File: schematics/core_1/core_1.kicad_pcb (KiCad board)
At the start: 2 copper layers, 100 x 91.1 mm, 22 parts, among them U1 74LS00, U2 74LS04, U3 74LS109, U4 74LS02

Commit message: power change
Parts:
- moved C5 1.90 mm to (105.0, 118.2)
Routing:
- net VCC: track 89.9 -> 119.0 mm, vias 1 -> 7
- net GND: track 151.6 -> 153.6 mm
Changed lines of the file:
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@@
 	(footprint "Capacitor_THT:C_Radial_D6.3mm_H5.0mm_P2.50mm"
 		(layer "F.Cu")
-		(at 106.8 118.85 90)
+		(at 105 118.240522 90)
 		(descr "C, Radial series, Radial, pin pitch=2.50mm, diameter=6.3mm, height=5mm, Non-Polar Electrolytic Capacitor")
 		(tags "C Radial series Radial pin pitch 2.50mm diameter 6.3mm height 5mm Non-Polar Electrolytic Capacitor")
@@
 	)
 	(segment
+		(start 104 122.75)
+		(end 104 126.5)
+		(width 0.6)
+		(layer "F.Cu")
+		(net 2)
+	)
+	(segment
+		(start 106 122.75)
+		(end 106 126.5)
+		(width 0.6)
+		(layer "F.Cu")
+		(net 2)
+	)
+	(segment
+		(start 105 122.75)
+		(end 105 126.5)
+		(width 0.6)
+		(layer "F.Cu")
+		(net 2)
+	)
+	(segment
 		(start 190.56 57.05)
 		(end 190.56 53.01)
@@
 	)
 	(segment
+		(start 103.25 122.75)
+		(end 103 123)
+		(width 0.3)
+		(layer "F.Cu")
+		(net 2)
+	)
+	(segment
+		(start 107 122.75)
+		(end 107 126.5)
+		(width 0.6)
+		(layer "F.Cu")
+		(net 2)
+	)
+	(segment
+		(start 105 122.75)
+		(end 105 118.240522)
+		(width 0.6)
+		(layer "F.Cu")
+		(net 2)
+	)
+	(segment
 		(start 178.2 103.2)
 		(end 178.78 102.62)
@@
 	)
 	(segment
+		(start 103 123)
+		(end 103 126.5)
+		(width 0.3)
+		(layer "F.Cu")
+		(net 2)
+	)
+	(segment
 		(start 122 75.68)
 		(end 122 71.65)
@@
 	)
 	(segment
+		(start 107 122.75)
+		(end 103.25 122.75)
+		(width 0.6)
+		(layer "F.Cu")
+		(net 2)
+	)
+	(segment
 		(start 191.7 79.95)
 		(end 191 79.25)
@@
 	)
 	(via
-		(at 105 121.1)
-		(size 0.8)
-		(drill 0.4)
+		(at 104 122.75)
+		(size 0.6)
+		(drill 0.3)
 		(layers "F.Cu" "B.Cu")
-		(free yes)
 		(net 2)
 	)
-	(segment
-		(start 105 121.1)
-		(end 105 121.7)
-		(width 0.6)
-		(layer "B.Cu")
+	(via
+		(at 105 119.75)
+		(size 0.6)
+		(drill 0.3)
+		(layers "F.Cu" "B.Cu")
 		(net 2)
 	)
-	(segment
-		(start 106 122.1)
-		(end 107 123.1)
-		(width 0.6)
-		(layer "B.Cu")
+	(via
+		(at 103.25 122.75)
+		(size 0.6)
+		(drill 0.3)
+		(layers "F.Cu" "B.Cu")
+		(net 2)
+	)
+	(via
+		(at 105 122.75)
+		(size 0.6)
+		(drill 0.3)
+		(layers "F.Cu" "B.Cu")
+		(net 2)
+	)
+	(via
+		(at 105 121.25)
+		(size 0.6)
+		(drill 0.3)
+		(layers "F.Cu" "B.Cu")
+		(net 2)
+	)
+	(via
+		(at 106 122.75)
+		(size 0.6)
+		(drill 0.3)
+		(layers "F.Cu" "B.Cu")
+		(net 2)
+	)
+	(via
+		(at 107 122.75)
+		(size 0.6)
+		(drill 0.3)
+		(layers "F.Cu" "B.Cu")
 		(net 2)
 	)
 	(segment
-		(start 104 123)
-		(end 103.151 123.849)
+		(start 103.25 122.75)
+		(end 103.151 122.849)
 		(width 0.3)
 		(layer "B.Cu")
@@
 	)
 	(segment
-		(start 107 123.1)
-		(end 107 126.5)
+		(start 107 122.75)
+		(end 104 122.75)
 		(width 0.6)
 		(layer "B.Cu")
@@
 	)
 	(segment
-		(start 106 126.5)
-		(end 106 122.1)
+		(start 105 121.25)
+		(end 105 119.75)
 		(width 0.6)
 		(layer "B.Cu")
@@
 	)
 	(segment
-		(start 105 121.1)
-		(end 106 122.1)
+		(start 106 126.5)
+		(end 106 122.75)
 		(width 0.6)
 		(layer "B.Cu")
@@
 	)
 	(segment
-		(start 103.151 123.849)
+		(start 103.151 122.849)
 		(end 103.151 125.95)
 		(width 0.3)
@@
 	)
 	(segment
-		(start 105 121.7)
-		(end 105 126.5)
+		(start 107 122.75)
+		(end 107 126.5)
+		(width 0.6)
+		(layer "B.Cu")
+		(net 2)
+	)
+	(segment
+		(start 104 122.75)
+		(end 103.25 122.75)
 		(width 0.6)
 		(layer "B.Cu")
@@
 	)
 	(segment
-		(start 105 121.8)
-		(end 104 122.8)
+		(start 105 119.75)
+		(end 105 118.240522)
+		(width 0.6)
+		(layer "B.Cu")
+		(net 2)
+	)
+	(segment
+		(start 105 122.75)
+		(end 105 121.25)
+		(width 0.6)
+		(layer "B.Cu")
+		(net 2)
+	)
+	(segment
+		(start 105 122.75)
+		(end 105 126.5)
 		(width 0.6)
 		(layer "B.Cu")
@@
 	)
 	(segment
-		(start 116.051 124.949)
-		(end 116.051 126.5)
-		(width 0.2)
-		(layer "F.Cu")
-		(net 6)
-	)
-	(segment
 		(start 145 126.5)
 		(end 145 123.25)
@@
 	)
 	(segment
+		(start 116.051 123.949)
+		(end 116.051 126.5)
+		(width 0.2)
+		(layer "F.Cu")
+		(net 6)
+	)
+	(segment
 		(start 163 124)
 		(end 163.5 123.5)
@@
 	)
 	(segment
-		(start 117 124)
-		(end 116.051 124.949)
-		(width 0.2)
-		(layer "F.Cu")
-		(net 6)
-	)
-	(segment
 		(start 173.5 123.5)
 		(end 174.5 123.5)
@@
 	)
 	(segment
+		(start 117 123)
+		(end 116.051 123.949)
+		(width 0.2)
+		(layer "F.Cu")
+		(net 6)
+	)
+	(segment
 		(start 168 126.5)
 		(end 168 124)
@@
 	)
 	(segment
-		(start 116.051 124.949)
-		(end 116.051 126.5)
-		(width 0.2)
-		(layer "B.Cu")
-		(net 6)
-	)
-	(segment
-		(start 117 124)
-		(end 116.051 124.949)
-		(width 0.2)
-		(layer "B.Cu")
-		(net 6)
-	)
-	(segment
 		(start 179 123.75)
 		(end 178.5 123.25)
@@
 	)
 	(segment
+		(start 116.051 123.949)
+		(end 116.051 126.5)
+		(width 0.2)
+		(layer "B.Cu")
+		(net 6)
+	)
+	(segment
 		(start 174.75 123.25)
 		(end 175.5 123.25)
@@
 	)
 	(segment
+		(start 117 123)
+		(end 116.051 123.949)
+		(width 0.2)
+		(layer "B.Cu")
+		(net 6)
+	)
+	(segment
 		(start 193.597 109.403)
 		(end 193.597 65.167)
@@
 		(polygon
 			(pts
-				(xy 95.5 31) (xy 95.75 127.052027) (xy 194.304731 126.950425) (xy 194.25 30.750005)
+				(xy 95.5 31) (xy 95.734108 120.946125) (xy 194.301257 120.844509) (xy 194.25 30.750005)
 			)
 		)

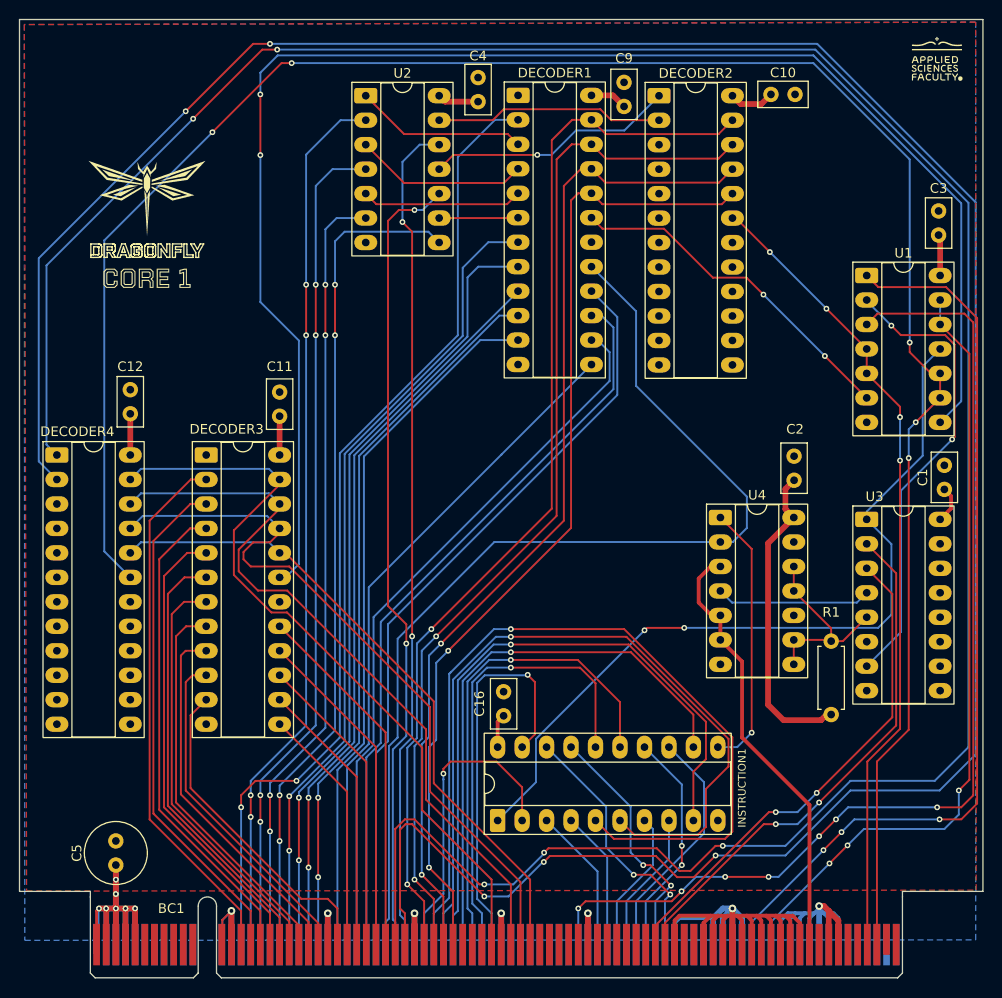
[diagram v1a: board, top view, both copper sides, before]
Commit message: fix: removed in control pins daisy chains
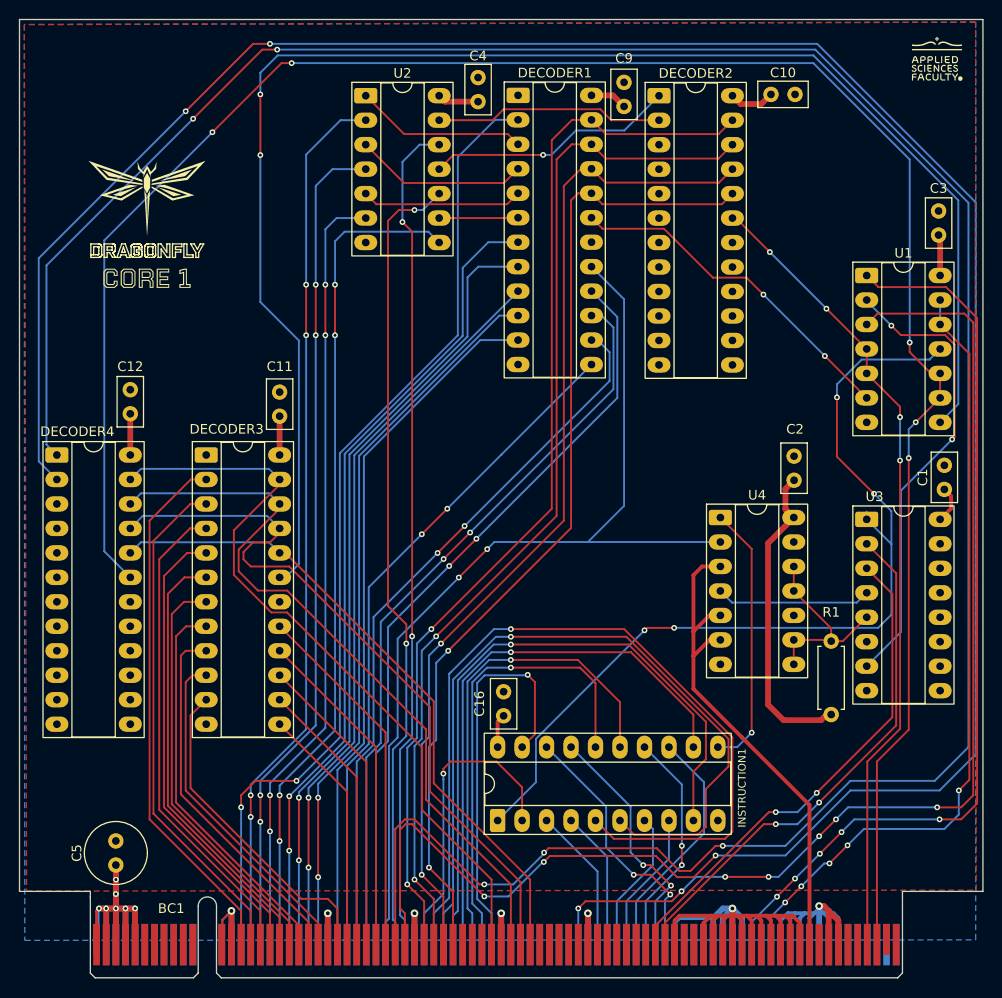
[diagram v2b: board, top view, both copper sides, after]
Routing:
- net /~{Reset}: track 84.2 -> 95.3 mm, vias 2 -> 4
- net /~{Clk}: track 46.4 -> 53.5 mm
- net /~{InstructionReader}: track 107.1 -> 101.5 mm, vias 0 -> 2
- net /Reset: track 81.6 -> 81.9 mm, vias 3 -> 5
- net /~{ZHReader}: vias 0 -> 2
- net /~{FlagsReader}: vias 0 -> 2
- net /~{ZLReader}: vias 0 -> 2
- net /~{YHReader}: vias 0 -> 2
- net /IRQ: vias 3 -> 5

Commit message: fix(alu, core_1_2, interface): put vcc zones on back layer
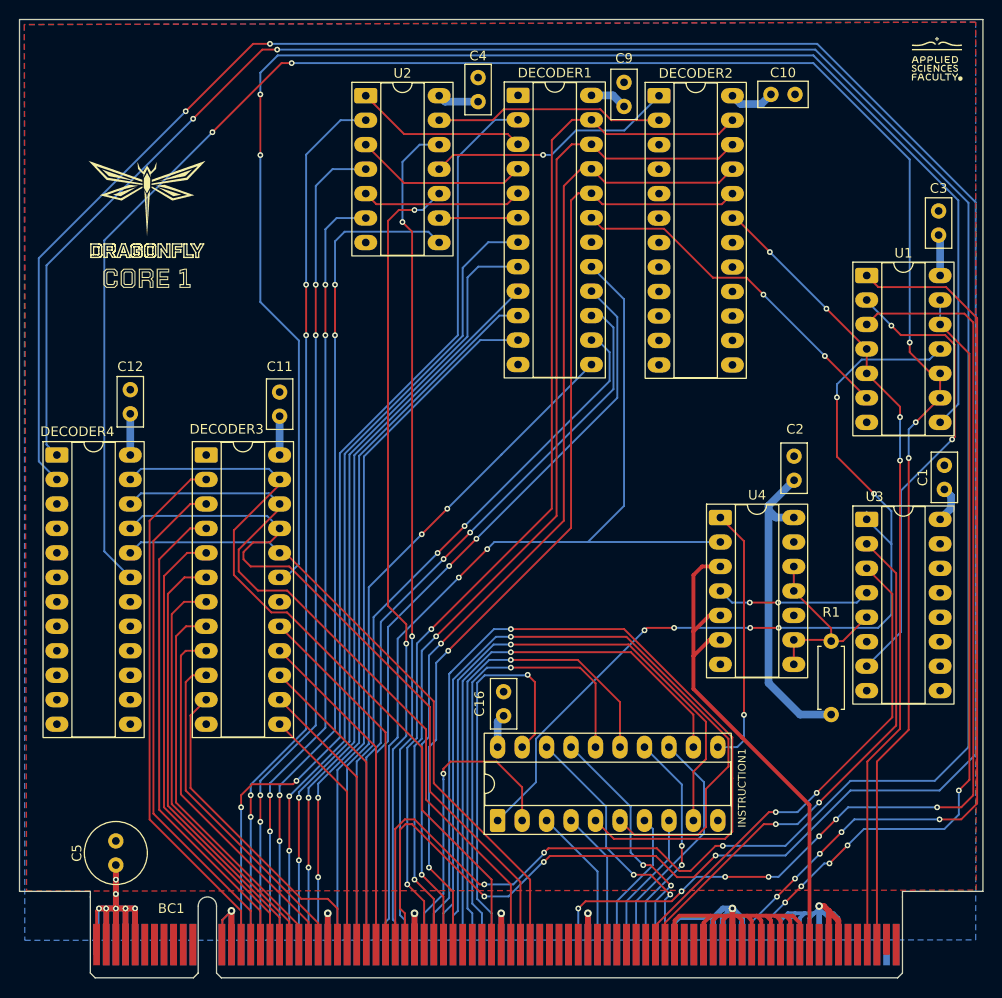
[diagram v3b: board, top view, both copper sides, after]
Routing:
- net VCC: track 119.0 -> 119.9 mm
- net Net-(INSTRUCTION1-Cp): track 27.8 -> 27.1 mm
- net Net-(U3A-C): vias 0 -> 2
- net /~{Reset}: vias 4 -> 6

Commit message: slight changes to vcc
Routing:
- net VCC: track 119.9 -> 90.8 mm
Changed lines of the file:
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@@
 	)
 	(segment
-		(start 172.75 80.95)
-		(end 172.75 81.4)
+		(start 175.4 78.3)
+		(end 175.4 82.14)
 		(width 0.8)
 		(layer "B.Cu")
@@
 	)
 	(segment
-		(start 173.52 82.17)
-		(end 172.75 81.4)
-		(width 0.8)
-		(layer "B.Cu")
-		(net 2)
-	)
-	(segment
 		(start 106.5 75.68)
 		(end 106.5 71.4)
-		(width 0.8)
-		(layer "B.Cu")
-		(net 2)
-	)
-	(segment
-		(start 175.4 78.3)
-		(end 172.75 80.95)
 		(width 0.8)
 		(layer "B.Cu")
@@
 	)
 	(segment
-		(start 172.75 99.35)
-		(end 176.02 102.62)
-		(width 0.8)
-		(layer "B.Cu")
-		(net 2)
-	)
-	(segment
 		(start 103.151 122.849)
 		(end 103.151 125.95)
@@
 	)
 	(segment
-		(start 172.75 81.4)
-		(end 172.75 99.35)
-		(width 0.8)
-		(layer "B.Cu")
-		(net 2)
-	)
-	(segment
 		(start 107 122.75)
 		(end 107 126.5)
 		(width 0.6)
-		(layer "B.Cu")
-		(net 2)
-	)
-	(segment
-		(start 175.37 82.17)
-		(end 173.52 82.17)
-		(width 0.8)
 		(layer "B.Cu")
 		(net 2)
@@
 		(start 122 75.68)
 		(end 122 71.65)
-		(width 0.8)
-		(layer "B.Cu")
-		(net 2)
-	)
-	(segment
-		(start 176.02 102.62)
-		(end 179.25 102.62)
 		(width 0.8)
 		(layer "B.Cu")
@@
 		(layer "B.Cu")
 		(net 2)
+	)
+	(segment
+		(start 175.4 82.14)
+		(end 175.37 82.17)
+		(width 0.8)
+		(layer "B.Cu")
+		(net 2)

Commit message: slight changes
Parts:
- moved R1 15.4 mm to (179.2, 87.2), turned to -90 degrees
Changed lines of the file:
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@@
 	(footprint "Resistor_THT:R_Axial_DIN0207_L6.3mm_D2.5mm_P7.62mm_Horizontal"
 		(layer "F.Cu")
-		(at 179.25 102.62 90)
+		(at 179.25 87.25 -90)
 		(descr "Resistor, Axial_DIN0207 series, Axial, Horizontal, pin pitch=7.62mm, 0.25W = 1/4W, length*diameter=6.3*2.5mm^2, http://cdn-reichelt.de/documents/datenblatt/B400/1_4W%23YAG.pdf")
 		(tags "Resistor Axial_DIN0207 series Axial Horizontal pin pitch 7.62mm 0.25W = 1/4W length 6.3mm diameter 2.5mm")
 		(property "Reference" "R1"
-			(at 10.62 0 180)
+			(at 10.62 0 0)
 			(layer "F.SilkS")
 			(effects
@@
 		(attr through_hole)
 		(fp_line
-			(start 7.08 -1.37)
-			(end 7.08 -1.04)
+			(start 0.54 1.37)
+			(end 7.08 1.37)
 			(stroke
 				(width 0.12)
@@
 		)
 		(fp_line
-			(start 0.54 -1.37)
-			(end 7.08 -1.37)
+			(start 7.08 1.37)
+			(end 7.08 1.04)
 			(stroke
 				(width 0.12)
@@
 		)
 		(fp_line
-			(start 0.54 -1.04)
-			(end 0.54 -1.37)
+			(start 0.54 1.04)
+			(end 0.54 1.37)
 			(stroke
 				(width 0.12)
@@
 		)
 		(fp_line
-			(start 0.54 1.04)
-			(end 0.54 1.37)
+			(start 0.54 -1.04)
+			(end 0.54 -1.37)
 			(stroke
 				(width 0.12)
@@
 		)
 		(fp_line
-			(start 7.08 1.37)
-			(end 7.08 1.04)
+			(start 0.54 -1.37)
+			(end 7.08 -1.37)
 			(stroke
 				(width 0.12)
@@
 		)
 		(fp_line
-			(start 0.54 1.37)
-			(end 7.08 1.37)
+			(start 7.08 -1.37)
+			(end 7.08 -1.04)
 			(stroke
 				(width 0.12)
@@
 		)
 		(fp_line
-			(start 7.62 0)
-			(end 6.96 0)
+			(start 0 0)
+			(end 0.66 0)
 			(stroke
 				(width 0.1)
@@
 		)
 		(fp_line
-			(start 0 0)
-			(end 0.66 0)
+			(start 7.62 0)
+			(end 6.96 0)
 			(stroke
 				(width 0.1)
@@
 		)
 		(pad "1" thru_hole circle
-			(at 0 0 90)
+			(at 0 0 270)
 			(size 1.6 1.6)
 			(drill 0.8)
@@
 		)
 		(pad "2" thru_hole circle
-			(at 7.62 0 90)
+			(at 7.62 0 270)
 			(size 1.6 1.6)
 			(drill 0.8)
@@
 	)
 	(segment
-		(start 178.78 102.62)
-		(end 179.25 102.62)
-		(width 0.6)
-		(layer "F.Cu")
-		(net 2)
-	)
-	(segment
 		(start 104 122.75)
 		(end 104 126.5)
@@
 	(segment
 		(start 177 126.5)
-		(end 177 112)
+		(end 177 110)
 		(width 0.4)
 		(layer "F.Cu")
@@
 	)
 	(segment
-		(start 165.85 87.25)
-		(end 167.75 87.25)
+		(start 164.95 97.95)
+		(end 164.95 96.55)
 		(width 0.4)
 		(layer "F.Cu")
@@
 	)
 	(segment
-		(start 164.95 96.55)
-		(end 164.95 94)
+		(start 177 110)
+		(end 164.95 97.95)
 		(width 0.4)
 		(layer "F.Cu")
@@
 	)
 	(segment
-		(start 170 105)
-		(end 164.95 99.95)
+		(start 165.85 87.25)
+		(end 167.75 87.25)
 		(width 0.4)
 		(layer "F.Cu")
@@
 	)
 	(segment
-		(start 164.95 99.95)
-		(end 164.95 96.55)
+		(start 164.95 96.55)
+		(end 164.95 94)
 		(width 0.4)
 		(layer "F.Cu")
@@
 	)
 	(segment
-		(start 177 112)
-		(end 170 105)
-		(width 0.4)
-		(layer "F.Cu")
-		(net 38)
-	)
-	(segment
 		(start 167.75 94.87)
 		(end 166.63 94.87)
@@
 	)
 	(segment
-		(start 162.95 93.621)
-		(end 160.129 93.621)
+		(start 160.25 93.621)
+		(end 162.75 93.621)
 		(width 0.2)
 		(layer "F.Cu")
@@
 		(net 135)
 	)
-	(segment
-		(start 160.129 93.621)
-		(end 159.875 93.875)
-		(width 0.2)
-		(layer "F.Cu")
-		(net 135)
-	)
 	(via
 		(at 173.8 93.621)
@@
 	)
 	(via
-		(at 162.95 93.621)
+		(at 162.75 93.621)
 		(size 0.6)
 		(drill 0.3)
@@
 	)
 	(via
-		(at 159.875 93.875)
+		(at 160.25 93.621)
 		(size 0.6)
 		(drill 0.3)
@@
 	)
 	(segment
-		(start 162.95 93.621)
-		(end 170.85 93.621)
-		(width 0.2)
-		(layer "B.Cu")
-		(net 135)
-	)
-	(segment
 		(start 185.5 92.25)
 		(end 185.5 84.92)
@@
 	)
 	(segment
-		(start 148.609 105.141)
-		(end 148.609 109.641)
+		(start 185.5 81.5)
+		(end 183.7 79.7)
 		(width 0.2)
 		(layer "B.Cu")
@@
 	)
 	(segment
-		(start 185.5 81.5)
-		(end 183.7 79.7)
+		(start 182.94 82.36)
+		(end 182.94 81.56)
 		(width 0.2)
 		(layer "B.Cu")
@@
 	)
 	(segment
-		(start 159.875 93.875)
-		(end 148.609 105.141)
+		(start 162.75 93.621)
+		(end 170.85 93.621)
 		(width 0.2)
 		(layer "B.Cu")
@@
 	)
 	(segment
-		(start 182.94 82.36)
-		(end 182.94 81.56)
+		(start 173.8 93.621)
+		(end 184.129 93.621)
 		(width 0.2)
 		(layer "B.Cu")
@@
 	)
 	(segment
-		(start 148.609 109.641)
-		(end 144.63 113.62)
+		(start 160.25 93.621)
+		(end 160.129 93.621)
 		(width 0.2)
 		(layer "B.Cu")
@@
 	)
 	(segment
-		(start 173.8 93.621)
-		(end 184.129 93.621)
+		(start 148.609 105.141)
+		(end 148.609 109.641)
+		(width 0.2)
+		(layer "B.Cu")
+		(net 135)
+	)
+	(segment
+		(start 160.129 93.621)
+		(end 148.609 105.141)
 		(width 0.2)
 		(layer "B.Cu")
@@
 	)
 	(segment
+		(start 148.609 109.641)
+		(end 144.63 113.62)
+		(width 0.2)
+		(layer "B.Cu")
+		(net 135)
+	)
+	(segment
 		(start 170.2 84.62)
 		(end 167.75 82.17)
@@
 	)
 	(segment
-		(start 170.2 102.65)
+		(start 170.2 101)
 		(end 170.2 84.62)
 		(width 0.2)
@@
 	)
 	(via
-		(at 170.2 102.65)
+		(at 170.2 101)
 		(size 0.6)
 		(drill 0.3)
@@
 	)
 	(segment
-		(start 170.2 102.65)
-		(end 170.2 105.3)
+		(start 169.5 106)
+		(end 167.49 106)
 		(width 0.2)
 		(layer "B.Cu")
@@
 	)
 	(segment
-		(start 170.2 105.3)
-		(end 169.5 106)
+		(start 170.2 101)
+		(end 170.2 105.3)
 		(width 0.2)
 		(layer "B.Cu")
@@
 	)
 	(segment
-		(start 169.5 106)
-		(end 167.49 106)
+		(start 170.2 105.3)
+		(end 169.5 106)
 		(width 0.2)
 		(layer "B.Cu")
@@
 	)
 	(segment
-		(start 175.37 94.87)
-		(end 179.12 94.87)
-		(width 0.2)
-		(layer "F.Cu")
-		(net 145)
-	)
-	(segment
 		(start 179.25 93.67)
 		(end 175.37 89.79)
@@
 	)
 	(segment
-		(start 179.12 94.87)
-		(end 179.25 95)
+		(start 179.25 94.87)
+		(end 180.59 94.87)
 		(width 0.2)
 		(layer "F.Cu")
@@
 	)
 	(segment
-		(start 179.25 95)
-		(end 179.25 93.67)
+		(start 180.59 94.87)
+		(end 182.94 92.52)
 		(width 0.2)
 		(layer "F.Cu")
@@
 	)
 	(segment
-		(start 175.37 97.41)
-		(end 175.37 94.87)
+		(start 175.37 94.87)
+		(end 179.25 94.87)
 		(width 0.2)
 		(layer "F.Cu")
@@
 	)
 	(segment
-		(start 175.37 89.79)
-		(end 175.37 87.25)
+		(start 179.25 94.87)
+		(end 179.25 93.67)
 		(width 0.2)
 		(layer "F.Cu")
@@
 	)
 	(segment
-		(start 180.46 95)
-		(end 182.94 92.52)
+		(start 175.37 97.41)
+		(end 175.37 94.87)
 		(width 0.2)
 		(layer "F.Cu")
@@
 	)
 	(segment
-		(start 179.25 95)
-		(end 180.46 95)
+		(start 175.37 89.79)
+		(end 175.37 87.25)
 		(width 0.2)
 		(layer "F.Cu")
